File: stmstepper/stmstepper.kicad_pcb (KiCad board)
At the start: 2 copper layers, 50 x 50 mm, 4 parts, among them J1 Conn_02x12, J2 Conn_02x12, J3 Conn_02x12, J4 Conn_02x12

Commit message: add stmstepper pcb
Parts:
- added J5: CONN_01X08, Socket_Strips:Socket_Strip_Straight_1x08_Pitch2.54mm, F.Cu at (130.3, 66.7)
- added J6: CONN_01X08, Socket_Strips:Socket_Strip_Straight_1x08_Pitch2.54mm, F.Cu at (143.0, 66.7)
- added J7: CONN_01X08, Socket_Strips:Socket_Strip_Straight_1x08_Pitch2.54mm, F.Cu at (150.6, 66.7)
- added J8: CONN_01X08, Socket_Strips:Socket_Strip_Straight_1x08_Pitch2.54mm, F.Cu at (163.3, 66.7)
- added JP1: Jumper_NC_Dual, Pin_Headers:Pin_Header_Straight_1x03_Pitch2.54mm, F.Cu at (183.6, 90.8)
- added JP2: Jumper, Pin_Headers:Pin_Header_Straight_1x02_Pitch2.54mm, F.Cu at (183.6, 99.7)
- added P1: CONN_01X02, Connectors_Molex:Molex_Microfit3_Header_02x02_Angled_43045-040x, F.Cu at (181.9, 47.2)
- added P2: CONN_01X04, Connectors_Molex:Molex_KK-6410-04_04x2.54mm_Straight, F.Cu at (132.8, 41.3)
- added P3: CONN_01X04, Connectors_Molex:Molex_KK-6410-04_04x2.54mm_Straight, F.Cu at (153.2, 41.3)
- added P4: CONN_01X05, Pin_Headers:Pin_Header_Straight_1x05_Pitch2.54mm, F.Cu at (122.7, 66.7)
- added P5: CONN_01X05, Pin_Headers:Pin_Header_Straight_1x05_Pitch2.54mm, F.Cu at (170.9, 66.7)
- added P6: Conn_02x03_Odd_Even, libs:CAN_Header, F.Cu at (181.1, 108.6)
- added R1: R120, Resistors_SMD:R_0805_HandSoldering, B.Cu at (155.1, 95.3)
- added U1: SN65HVD230, Housings_SOIC:SOIC-8_3.9x4.9mm_Pitch1.27mm, B.Cu at (154.4, 87.0)
- added U2: 7805, TO_SOT_Packages_THT:TO-220_Horizontal, F.Cu at (183.6, 80.7)
- J1, J2, J3, J4: value Conn_02x12 -> Conn_02x12_Odd_Even
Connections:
- J1 pad 1: (no net) -> /GPIO0
- J1 pad 10: (no net) -> /A-EN
- J1 pad 11: (no net) -> /GPIO10
- J1 pad 12: (no net) -> /B-EN
- J1 pad 13: (no net) -> /GPIO13
- J1 pad 14: (no net) -> /B-MS2
- J1 pad 15: (no net) -> /SPI3_MOSI
- J1 pad 16: (no net) -> /B-MS3
- J1 pad 17: (no net) -> /SPI3_MISO
- J1 pad 18: (no net) -> /CAN3_TX
- J1 pad 19: (no net) -> /SPI3_SCK
- J1 pad 20: (no net) -> /CAN3_RX
- J1 pad 21: (no net) -> Net-(J1-Pad21)
- J1 pad 3: (no net) -> /TIM4_CH2
- J1 pad 4: (no net) -> /GPIO11
- J1 pad 5: (no net) -> /QSPI_NCS
- J1 pad 6: (no net) -> /I2C1_SCL
- J1 pad 7: (no net) -> /QSPI_IO2
- J1 pad 8: (no net) -> /I2C1_SDA
- J1 pad 9: (no net) -> /QSPI_IO1
- J2 pad 1: (no net) -> /GPIO15
- J2 pad 10: (no net) -> /B-MS1
- J2 pad 11: (no net) -> /GPIO7
- J2 pad 12: (no net) -> /A-MS3
- J2 pad 13: (no net) -> /CAN1_TX
- J2 pad 14: (no net) -> /A-DIR
- J2 pad 15: (no net) -> /CAN1_RX
- J2 pad 16: (no net) -> /TIM4_CH1
- J2 pad 17: (no net) -> /UART5_TX
- J2 pad 18: (no net) -> /A-MS1
- J2 pad 19: (no net) -> /UART5_RX
- J2 pad 20: (no net) -> /A-MS2
- J2 pad 21: (no net) -> /VDD
- J2 pad 3: (no net) -> /TIM8_CH4
- J2 pad 4: (no net) -> /SWCLK
- J2 pad 5: (no net) -> /TIM8_CH3
- J2 pad 6: (no net) -> /SWDIO
- J2 pad 7: (no net) -> /TIM8_CH2
- J2 pad 8: (no net) -> /B-DIR
- J2 pad 9: (no net) -> /TIM8_CH1
- J3 pad 1: (no net) -> /TIM12_CH2
- J3 pad 10: (no net) -> /TIM1_CH2N
- J3 pad 11: (no net) -> /GPIO6
- J3 pad 12: (no net) -> /B-STEP
- J3 pad 13: (no net) -> /GPIO5
- J3 pad 14: (no net) -> /TIM1_CH1N
- J3 pad 15: (no net) -> /QSPI_CLK
- J3 pad 16: (no net) -> /A-STEP
- J3 pad 17: (no net) -> /ADC_IN14
- J3 pad 18: (no net) -> /SPI1_MOSI
- J3 pad 19: (no net) -> /SPI1_SCK
- J3 pad 20: (no net) -> /SPI1_MISO
- J3 pad 21: (no net) -> Net-(J3-Pad21)
- J3 pad 23: (no net) -> /DAC1_OUT
- J3 pad 3: (no net) -> /TIM12_CH1
- J3 pad 4: (no net) -> /TIM1_BKIN
- J3 pad 5: (no net) -> /I2C2_SCL
- J3 pad 6: (no net) -> /TIM1_CH3N
- J3 pad 7: (no net) -> /I2C2_SDA
- J3 pad 8: (no net) -> /TIM1_CH3
- J3 pad 9: (no net) -> /ADC_IN7
- J4 pad 1: (no net) -> /TIM3_CH4
- J4 pad 10: (no net) -> /NRST
- J4 pad 11: (no net) -> /SPI2_MISO
- J4 pad 12: (no net) -> /ADC_IN3
- J4 pad 13: (no net) -> /SPI2_SCK
- J4 pad 14: (no net) -> /ADC_IN2
- J4 pad 15: (no net) -> /GPIO4
- J4 pad 16: (no net) -> /VBAT
- J4 pad 17: (no net) -> /GPIO3
- J4 pad 18: (no net) -> /TIM9_CH2
- J4 pad 19: (no net) -> /GPIO2
- J4 pad 20: (no net) -> /TIM9_CH1
- J4 pad 21: (no net) -> Net-(J4-Pad21)
- J4 pad 23: (no net) -> /GPIO1
- J4 pad 3: (no net) -> /TIM2_CH2
- J4 pad 4: (no net) -> /TIM3_CH3
- J4 pad 5: (no net) -> /TIM2_CH1
- J4 pad 6: (no net) -> /ADC_IN13
- J4 pad 7: (no net) -> /ADC_IN10
- J4 pad 8: (no net) -> /ADC_IN15
- J4 pad 9: (no net) -> /SPI2_MOSI
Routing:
- net GND: track 0.00 -> 281.5 mm
- net /+3V3: track 0.00 -> 129.6 mm
- net /VDD: track 0.00 -> 117.2 mm
- net /VMOT: track 0.00 -> 93.0 mm
- net /EV: track 0.00 -> 77.7 mm
- net /A-MS1: track 0.00 -> 67.2 mm, vias 0 -> 1
- net /A-MS2: track 0.00 -> 66.7 mm, vias 0 -> 1
- net /B-STEP: track 0.00 -> 63.6 mm
- net /GPIO0: track 0.00 -> 58.3 mm
- net /A-STEP: track 0.00 -> 57.7 mm
- net /A-MS3: track 0.00 -> 54.3 mm, vias 0 -> 1
- net /B-MS1: track 0.00 -> 52.0 mm
- net /TIM2_CH2: track 0.00 -> 51.6 mm
- net /TIM4_CH2: track 0.00 -> 50.5 mm
- net /A-DIR: track 0.00 -> 49.5 mm, vias 0 -> 1
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- added copper zone on B.Cu, net GND
- added copper zone on F.Cu, net GND
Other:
- board size 50 x 50 mm -> 78.7 x 88.9 mm
- board text added: "+"
- board text added: "-"
- board text added: "3.3V"
- board text added: "CAN"
- board text added: "CAN TERMINATOR"
- board text added: "CH1"
- board text added: "CH2"
- board text added: "ENC1"
- board text added: "ENC2"
- board text added: "EV"
- board text added: "GND"
- board text added: "GPIO0"
- board text added: "GPIO3"
- board text added: "H"
- board text added: "L"
- board text added: "MOTOR A"
- board text added: "MOTOR B"
- board text added: "POWER"
- board text added: "VIN"

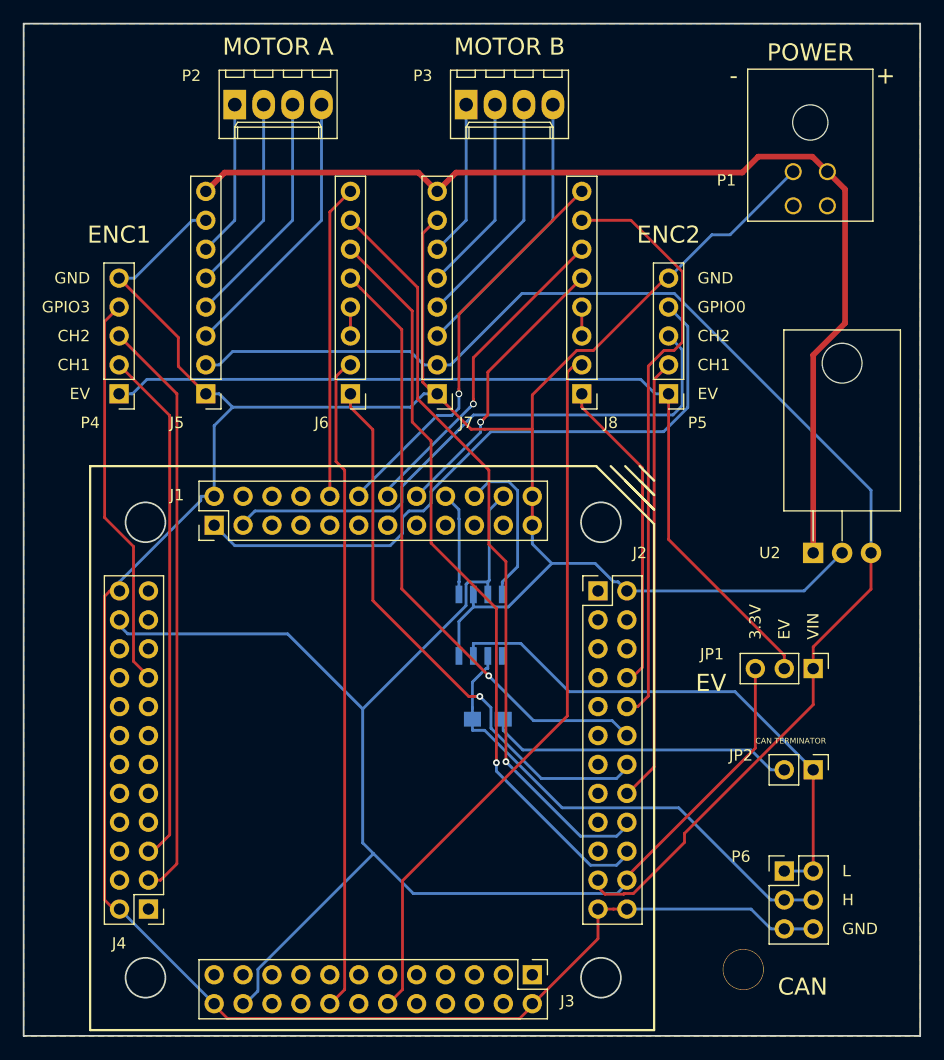
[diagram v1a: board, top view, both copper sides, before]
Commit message: final adjustments stmstepper, add logos
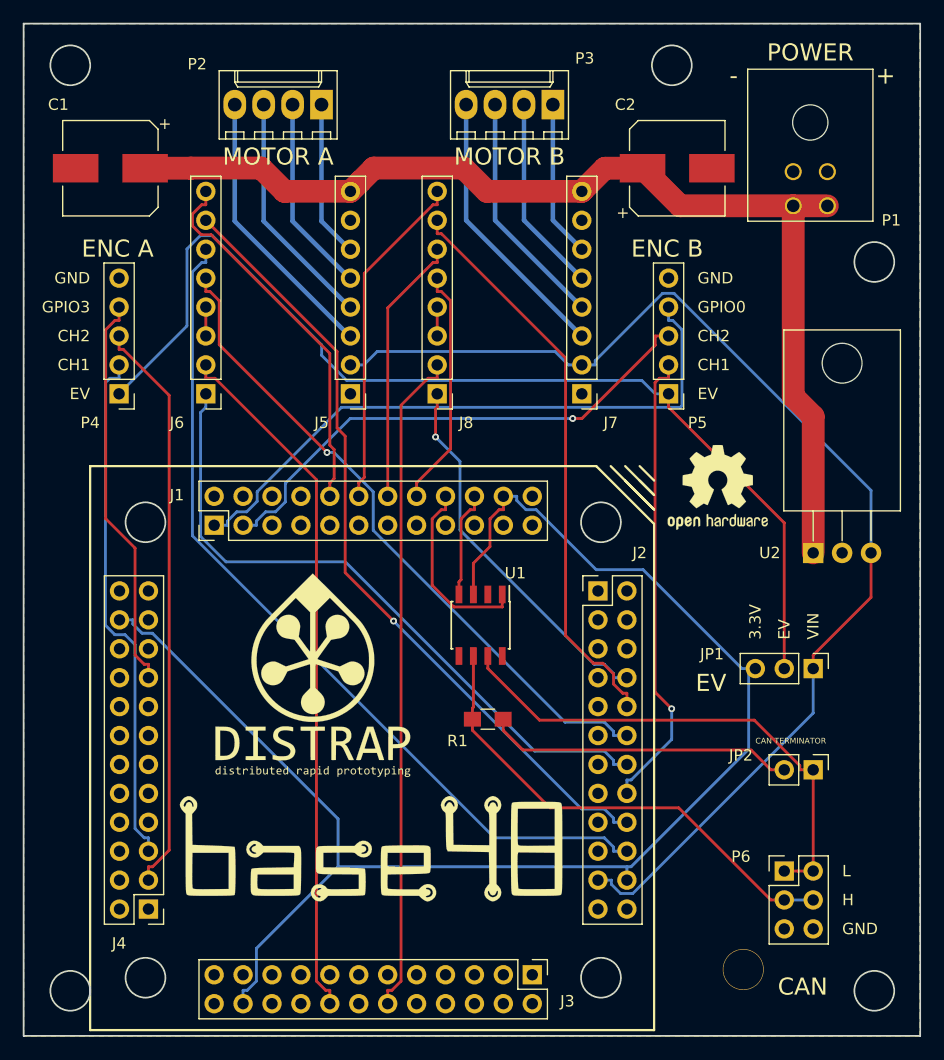
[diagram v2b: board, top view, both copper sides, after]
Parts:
- added C1: CP10u, Capacitors_SMD:CP_Elec_8x6.7, F.Cu at (121.9, 46.9)
- added C2: CP10u, Capacitors_SMD:CP_Elec_8x6.7, F.Cu at (171.7, 46.9)
- added G***: LOGO, libs:base48_34x9, F.Cu at (144.8, 106.7)
- added G01: LOGO, libs:distrap_qr_17x17, B.Cu at (139.7, 90.2)
- added G2: LOGO, libs:distrap_logo_full_17x18, F.Cu at (139.7, 91.4)
- added G4: LOGO, libs:distrap_logo_full_14x14, B.Cu at (154.9, 90.2)
- added G8: LOGO, libs:base48_34x9, B.Cu at (144.8, 106.7)
- added REF1: OSHW-Logo2_9.8x8mm_SilkScreen, Symbols:OSHW-Logo2_9.8x8mm_SilkScreen, F.Cu at (175.3, 74.9)
- added REF3: OSHW-Logo2_9.8x8mm_SilkScreen, Symbols:OSHW-Logo2_9.8x8mm_SilkScreen, B.Cu at (175.3, 106.7)
- P1: value CONN_01X02 -> Conn_01x04
- R1, U1: moved to F.Cu
- moved J5 12.7 mm to (143.0, 66.7)
- moved J6 12.7 mm to (130.3, 66.7)
- moved J7 12.7 mm to (163.3, 66.7)
- moved J8 12.7 mm to (150.6, 66.7)
- moved P2 7.62 mm to (140.5, 41.3), turned to 180 degrees
- moved P3 7.62 mm to (160.8, 41.3), turned to 180 degrees
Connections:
- P1 pad 2: /VMOT -> GND
- P1 pad 3: (no net) -> /VMOT
- P1 pad 4: (no net) -> /VMOT
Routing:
- net GND: track 281.5 -> 0.00 mm
- net /EV: track 77.7 -> 92.6 mm
- net /VDD: track 117.2 -> 104.5 mm
- net /A-DIR: track 49.5 -> 58.7 mm, vias 1 -> 0
- net /A-MS2: track 66.7 -> 75.7 mm, vias 1 -> 0
- net /CAN3_TX: track 9.13 -> 16.6 mm
- net /B-EN: track 35.6 -> 29.8 mm, vias 1 -> 0
- net /A-EN: track 27.5 -> 33.3 mm
- net /B-DIR: track 28.0 -> 33.2 mm, vias 0 -> 1
- net /B-MS2: track 28.8 -> 23.7 mm, vias 1 -> 0
- net /B-STEP: track 63.6 -> 58.6 mm
- net /CAN3_RX: track 14.3 -> 9.40 mm
- net /TIM4_CH2: track 50.5 -> 45.9 mm, vias 0 -> 1
- net /A-MS3: track 54.3 -> 58.8 mm
- net /+3V3: track 129.6 -> 133.7 mm
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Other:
- outline, holes or cut-outs redrawn
- net class motors added: clearance 0.2, trace_width 0.4, via_dia 0.6, via_drill 0.4
- net class my: trace_width 0.5 -> 2
- board text added: "ENC A"
- board text added: "ENC B"
- board text removed: "ENC1"
- board text removed: "ENC2"

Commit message: final fixes, add gerber files
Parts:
- moved U1 31.7 mm to (175.8, 110.5), turned to 0 degrees
- moved R1 25.4 mm to (178.8, 104.4)
- moved P6 1.88 mm to (182.9, 109.2)
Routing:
- net /CAN3_RX: track 9.40 -> 48.1 mm
- net /CAN3_TX: track 16.6 -> 47.7 mm
- net Net-(JP2-Pad1): track 45.0 -> 17.0 mm
- net Net-(P6-Pad3): track 42.7 -> 14.9 mm
- net Net-(JP2-Pad2): track 27.1 -> 5.04 mm
- net /EV: track 92.6 -> 77.7 mm
- net /A-MS1: track 70.1 -> 84.0 mm, vias 1 -> 0
- net /A-MS3: track 58.8 -> 69.2 mm
- net /VDD: track 104.5 -> 97.7 mm
- net /GPIO0: track 55.5 -> 50.4 mm, vias 0 -> 1
- net /TIM4_CH2: track 45.9 -> 50.4 mm, vias 1 -> 0
- net /B-DIR: track 33.2 -> 36.9 mm
- net /A-EN: track 33.3 -> 31.5 mm
- net /TIM4_CH1: track 41.0 -> 39.8 mm, vias 1 -> 0
- net /A-MS2: track 75.7 -> 76.3 mm, vias 0 -> 1
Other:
- net class motors: trace_width 0.4 -> 0.8
